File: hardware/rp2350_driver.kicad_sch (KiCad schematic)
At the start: 319 parts, among them J1 XT30, J10 Power Output, J11 CAN2 PLUG, J12 Conn_01x06, J2 XT30, J3 USB_C_Receptacle_USB2.0, J4 SM03B-SRSS-TB, J5 Estop Conn, J6 SM03B-SRSS-TB, J7 Conn_01x03, J8 Conn_01x03, J9 XT30, Q1 Q_PNP_BEC, Q2 Q_PNP_BEC, Q3 Q_PNP_BEC, Q4 Q_PNP_BEC, Q5 Q_NMOS_GDS, Q6 2N7002, SW1 Button, SW2 Button, U1 EG3113, U10 INA240A1D, U101 FUSB302BMPX, U11 USBLC6-2P6, U12 EG3113, U13 TS5A3159DCK, U14 TS5A3159DCK, U15 TS5A3159DCK, U16 CA-IS3052CG, U17 TS5A3159DCK, U18 SIT3088ETK, U19 SIT3088ETK, U20 SIT3088ETK, U21 SIT3088ETK, U22 TS5A3159DCK, U23 TS5A3159DCK, U24 TS5A3159DCK, U25 TS5A3159DCK, U26 TS5A3159DCK, U27 TS5A3159DCK, U28 XL7005A, U29 LM74700, U3 W25Q16JV, U30 TS5A3159DCK, U31 TS5A3159DCK, U32 TS5A3159DCK, U33 TS5A3159DCK, U4 SPX3819M5-L-3-3, U5 INA240A1D, U6 EG3113, U7 EG3113, U8 RP2350_80QFN, U9 INA240A1D, Y1 ABM8-272-T3

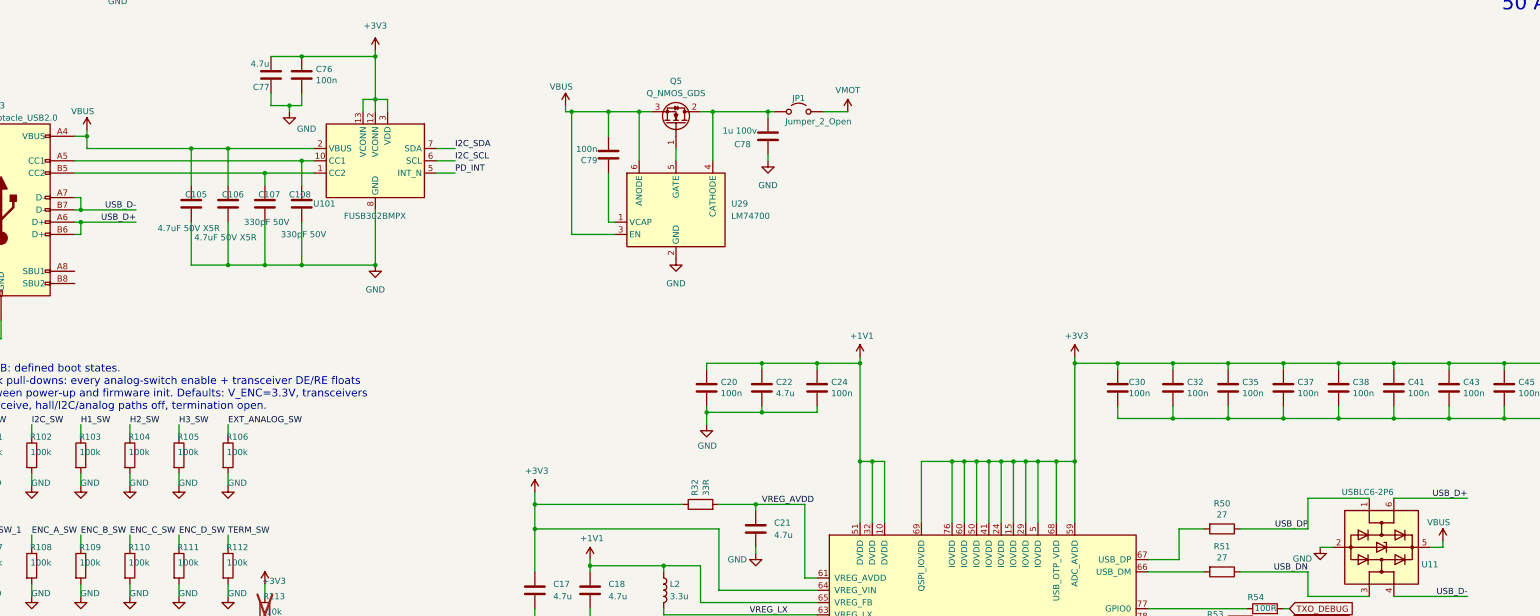
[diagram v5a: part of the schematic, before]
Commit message: rev-B schematic: LTC4359 USB power path (F-27) + U11/VBUS clamp fix (F-39)
First hardware change of the new rev. Both findings were rescoped to
rev-B on 2026-08-10 because the board's declared 5 A USB-PD capability
makes them shipping blockers, not respin nice-to-haves.

F-27 - the 65 V LM74700 was the weakest silicon on a 60 V bus, and at
5 A its companion FET was also a thermal fault:

  U29  LM74700 (SOT-23-6, 65 V abs max)  -> LTC4359CMS8 (MSOP-8, 4-80 V
       operating, 100 V abs-max pins, C688235)
  Q5   TMG08N10SI (SOT-89, 100 mohm, 2.5 W at 5 A)
       -> E100N4P0HL1 (PDFN5x6, 100 V, 4 mohm, 83 A, C29781176) ~0.1 W
  C79  removed - it was the LM74700 charge-pump cap; the LTC4359's pump
       is internal and the part needs no external cap here

Wired per the LTC4359 datasheet ideal-diode application: IN, SOURCE and
SHDN all at the input supply (SHDN tied to IN because shutdown is
unused, and the pin is rated to 100 V), GATE to the FET gate, OUT to
the drain, VSS to GND. FET orientation is unchanged - source to VBUS,
drain to the JP1/VMOT node - so the body diode still blocks backfeed.
Q5 moves to Device:Q_NMOS_SGD on parts:PowerPAK_SO-8_123, the same
symbol/footprint pair the bridge FETs use; the datasheet confirms
pins 1-3 = S, 4 = G, 5-8 = D, which is exactly that footprint's pad
numbering.

F-39 - U11 (USBLC6-2P6) referenced its data clamps to VBUS, a 5.5 V
abs-max pin sitting on a rail PD takes to 20 V:

  U11 pin 5 VBUS -> +3V3 (data lines clamp at ~4 V, correct for USB 2.0
      signalling, and the rail is always up when USB is active)
  D31 new SMAJ24A on VBUS at J3 (400 W, 24 V standoff, SMA, C148222),
      cathode to VBUS, anode to GND

Verified with kicad-cli: the net-level diff against the shipped rev-B
schematic contains these changes and nothing else, and ERC holds at the
baseline 278 violations (all pre-existing library-link noise).

Co-Authored-By: Claude Fable 5 <noreply@anthropic.com>
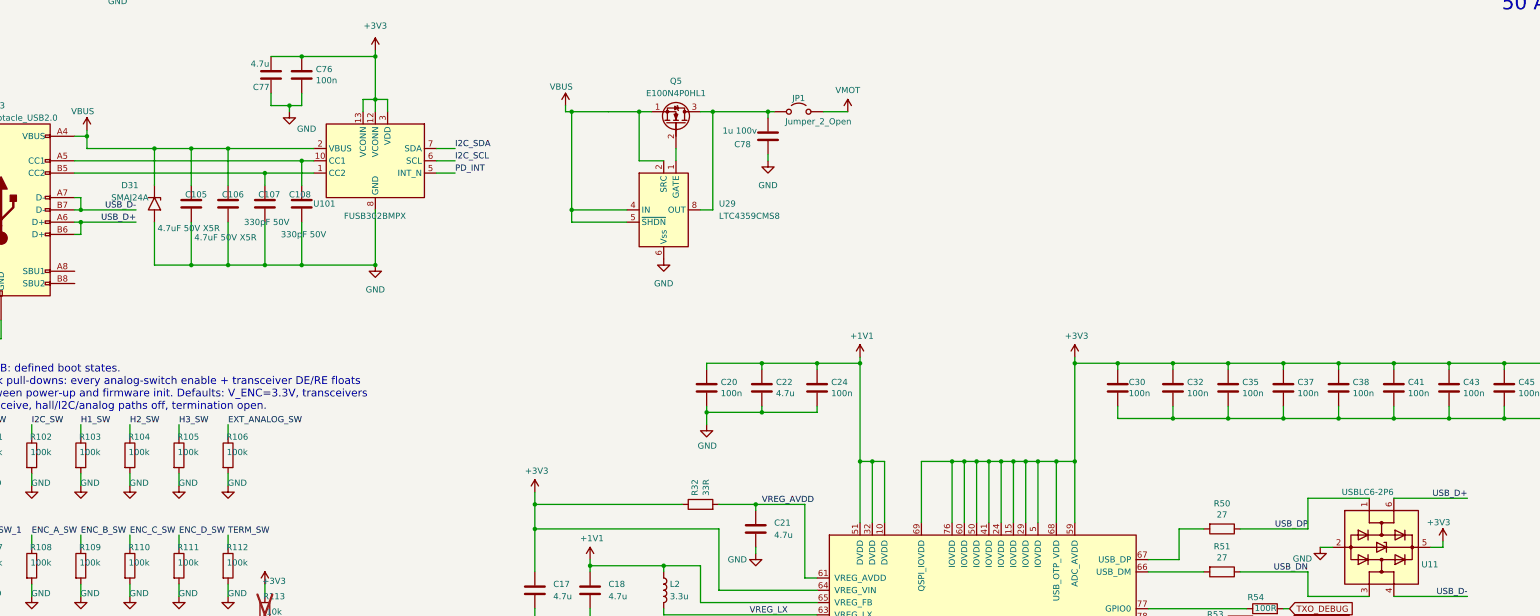
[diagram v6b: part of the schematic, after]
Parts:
- removed C79: 100n, Capacitor_SMD:C_0402_1005Metric, symbol Device:C
- added D31: SMAJ24A, Diode_SMD:D_SMA, symbol Diode:SMAJ24A
- Q5: value Q_NMOS_GDS -> E100N4P0HL1; footprint Package_TO_SOT_SMD:SOT-89-3 -> parts:PowerPAK_SO-8_123; symbol Transistor_FET:Q_NMOS_GDS -> Device:Q_NMOS_SGD; LCSC C7422896 -> C29781176
- U29: value LM74700 -> LTC4359CMS8; footprint Package_TO_SOT_SMD:SOT-23-6 -> Package_SO:MSOP-8_3x3mm_P0.65mm; symbol Power_Management:LM74700 -> Power_Management:LTC4359-MS8; LCSC C2941042 -> C688235
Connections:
- net +3V3: now also U11.5 (VBUS)
- net GND: now also U29.6 (Vss), D31.2 (A2); no longer U29.2 (GND)
- net VBUS: now also Q5.1 (S), U29.2 (SRC), U29.4 (IN), U29.5 (~{SHDN}), D31.1 (A1); no longer Q5.3 (S), U11.5 (VBUS), U29.3 (EN), U29.6 (ANODE)
- net at C78.2, JP1.1 (A): now also Q5.3 (D), U29.8 (OUT); no longer Q5.2 (D), U29.4 (CATHODE)
- net at U29.1 (GATE): now also Q5.2 (G)
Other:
- moved on the sheet: U29

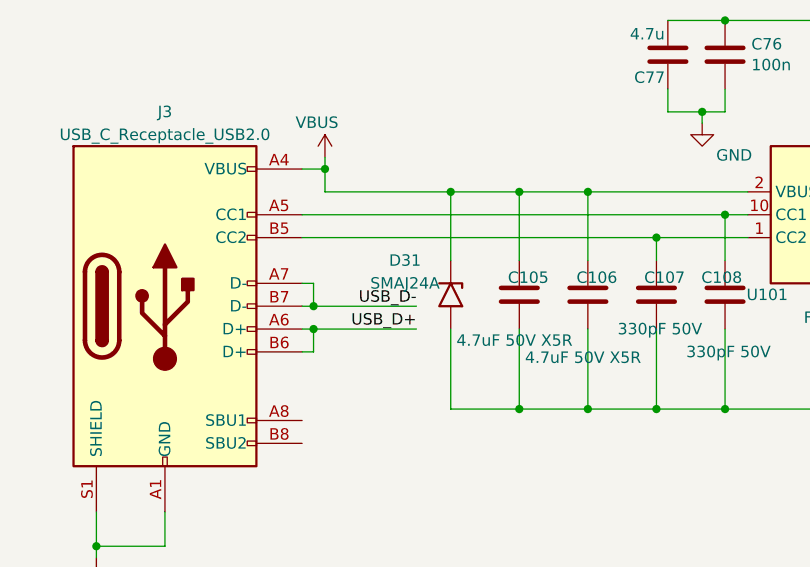
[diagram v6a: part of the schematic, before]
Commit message: rev-B PCB: sync F-27/F-39 to the schematic + placement (routing still due)
The schematic side of F-27/F-39 landed in 7058e41 with the PCB deliberately
left alone, on the read that both new footprints collided with five real
neighbours each and needed a placement session. That read was wrong: it counted
courtyards on the OPPOSITE copper side. U29 and Q5 are B.Cu parts, and most of
what looked like a collision (C45, C21, C24, R32, L2, C18, C17, C30, R50, R51)
is on F.Cu, where a courtyard cannot clash. Same-side, the job is small.

kicad-cli has no "update PCB from schematic" and pcbnew's SWIG bindings expose
no BOARD_NETLIST_UPDATER, so the sync is explicit, in tools/revb/:

  check_sync.py  exports the schematic netlist and diffs components, footprint
                 assignments and per-pad nets against the board. It classifies
                 the shipped board's pre-existing noise (27 footprints with no
                 library nickname, stale symbol-name values, unconnected-pad
                 naming, board-only thermal pads) instead of drowning in it.
                 This is the acceptance test, and it now says IN SYNC.
  scan_place.py  pose search. Drops the real footprint on the board at every
                 0.25 mm / 90 deg pose and asks KiCad for courtyards and pad
                 geometry. Hard constraints (same-side courtyard of a real
                 part, any other-net pad, board edge) must be zero; other-net
                 track segments crossed are the cost, since each is copper
                 someone must route again.
  sync_pcb.py    applies the delta, then verifies and refills before writing.

Placement chosen:

  U29  LTC4359 MSOP-8 at (167.745, 95.825) rot 0 - 1.00 mm east of the old
       SOT-23-6 centroid, rotated to horizontal into the space C79 vacated.
       Zero courtyard conflicts, zero test-point moves, zero extra copper.
  Q5   PowerPAK SO-8 at (170.400, 103.325) rot 180 - source east toward J3,
       drain west toward JP1, 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
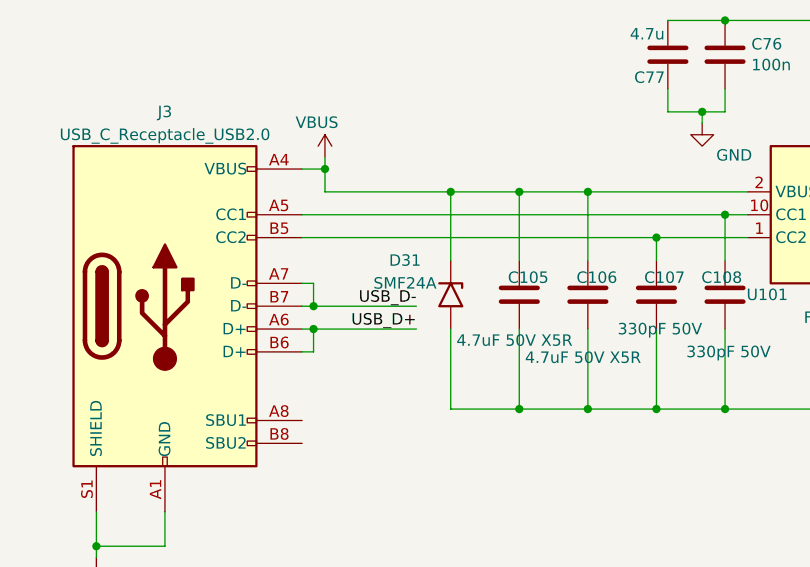
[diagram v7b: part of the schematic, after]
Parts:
- D31: value SMAJ24A -> SMF24A; footprint Diode_SMD:D_SMA -> Diode_SMD:D_SOD-123F; LCSC C148222 -> C169430
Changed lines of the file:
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@@
 			)
 		)
-		(property "Value" "SMAJ24A"
+		(property "Value" "SMF24A"
 			(at 93.98 104.14 90)
 			(effects
@@
 			)
 		)
-		(property "Footprint" "Diode_SMD:D_SMA"
+		(property "Footprint" "Diode_SMD:D_SOD-123F"
 			(at 99.06 105.41 90)
 			(effects
@@
 			)
 		)
-		(property "Datasheet" "https://www.littelfuse.com/media?resourcetype=datasheets&itemid=75e32973-b177-4ee3-a0ff-cedaf1abdb93&filename=smaj-datasheet"
+		(property "Datasheet" "https://www.littelfuse.com/assetdocs/tvs-diodes-smf-datasheet?assetguid=7eb8a5b6-bdd0-4561-8f19-0c3cc6f9b2af"
 			(at 99.06 105.41 0)
 			(effects
@@
 			)
 		)
-		(property "Description" "400W unidirectional TVS, 24 V standoff, SMA (DO-214AC) - VBUS surge clamp at J3"
+		(property "Description" "200W unidirectional TVS, 24 V standoff, SOD-123FL - VBUS surge clamp at J3"
 			(at 99.06 105.41 0)
 			(effects
@@
 			)
 		)
-		(property "LCSC" "C148222"
+		(property "LCSC" "C169430"
 			(at 99.06 105.41 0)
 			(effects

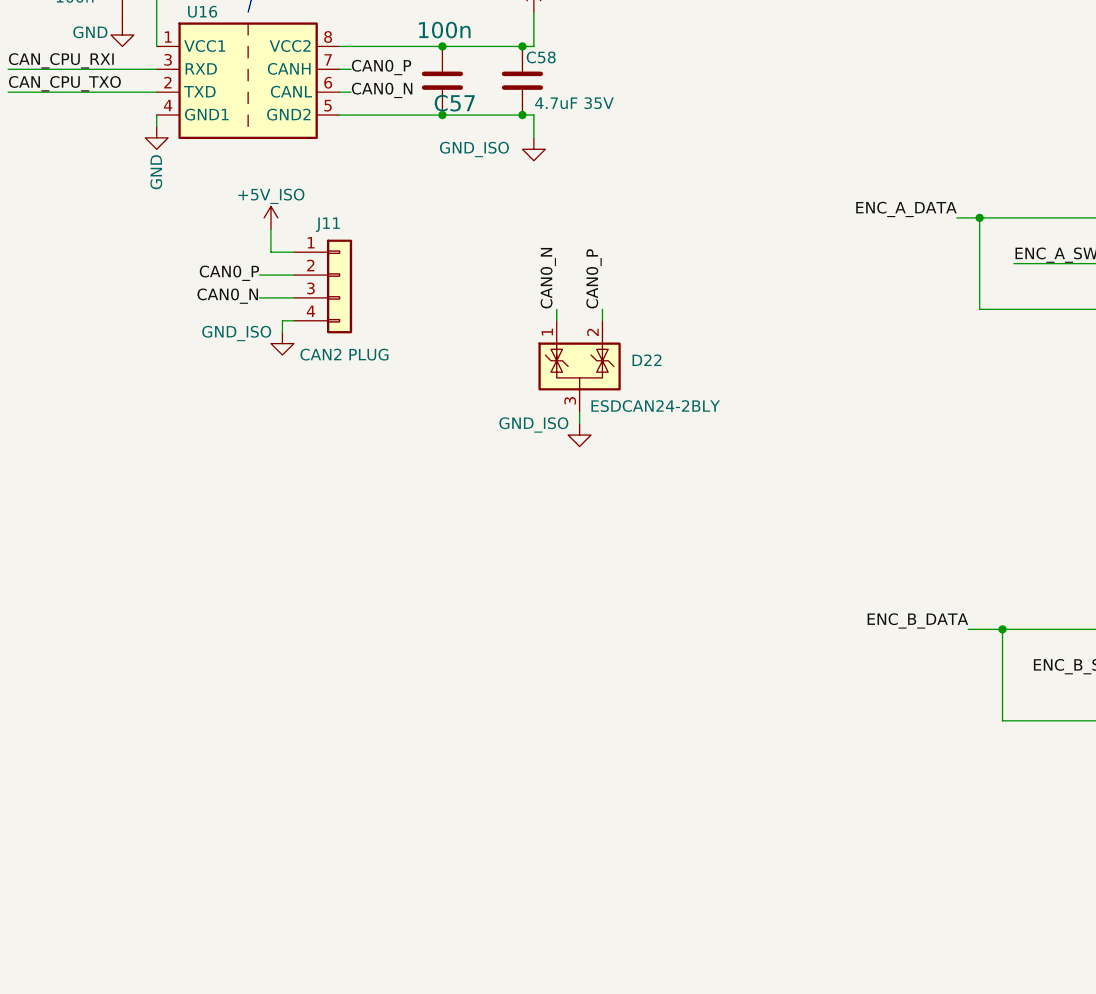
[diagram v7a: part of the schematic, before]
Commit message: rev-B: module-stretch verdict (F-44), rev-B parts re-placed + F-19 landed, Q6 SOT-23 (F-45), corner routed 238->54 airwires
Module stretch (review/modules.html, hardware/tools/modules/): the board carved
into 14 parent modules / 47 rigid leaves + 16 pinned interfaces; exact-polygon
slack probe, sequential-LP stretch, connectivity-owned copper warp, kicad DRC
referee. Verdict F-44: no module-level slack -- the DRC-neutral stretch is 5
loose parts (applied, signature-identical DRC); every dense-module move sheds
DRC violations through rule-pitch seam copper.

Placement: pose scanner on real KiCad geometry re-placed the 17 provisional
rev-B parts (U30-U33, C110-C113, R97-R100, R101/103/104/105/108), landed the
F-19 CAN parts (R114/JP2 by J11, C115 on the front between J11/J6, R115), and
swapped Q6 to the schematic's SOT-23 (F-45; check_sync known-exceptions now
empty). Corner cleanup removed the stray copper under the relaxed parts.

Routing: Freerouting with all copper locked hangs on this board; in-house
grid router (router.py) + GND plane stitching closed 197 of 251 connections.
Board: DRC 167 -> 4 (four cosmetic mask bridges), airwires 238 -> 54,
check_sync IN SYNC. F-25 stays open: the 54 left are named placement fixes.

Also lands the earlier uncommitted rev-B work on this branch: F-19 schematic
(add_f19_can_termination.py), F-43 0603->0402 shrink (shrink_0402.py), and
the F-19/F-42/F-43 register rows.

Co-Authored-By: Claude Fable 5 <noreply@anthropic.com>
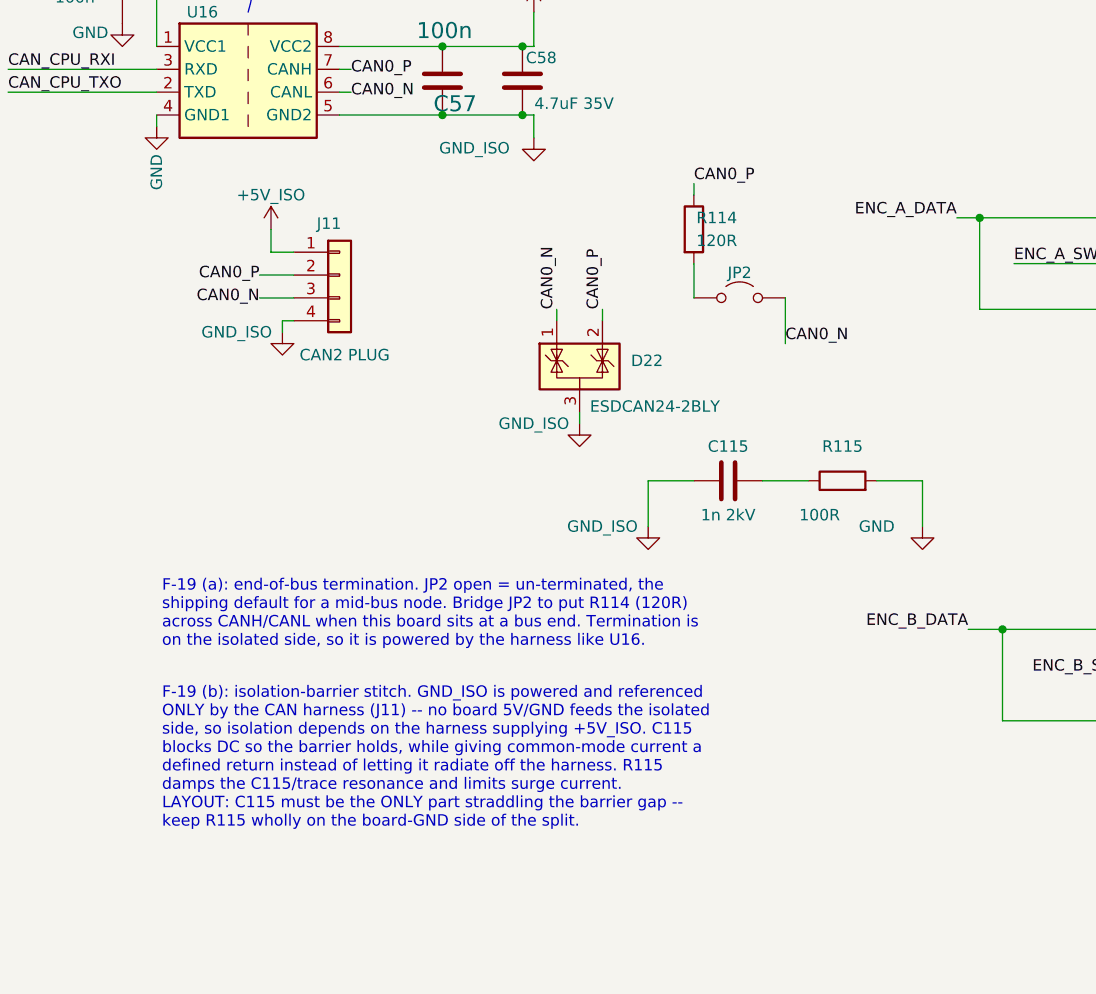
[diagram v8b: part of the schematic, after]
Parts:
- added C115: 1n 2kV, Capacitor_SMD:C_1206_3216Metric, symbol Device:C
- added JP2: Jumper_2_Open, Jumper:SolderJumper-2_P1.3mm_Open_RoundedPad1.0x1.5mm, symbol Jumper:Jumper_2_Open
- added R114: 120R, Resistor_SMD:R_0603_1608Metric, symbol Device:R
- added R115: 100R, Resistor_SMD:R_0603_1608Metric, symbol Device:R
- C16, C19, C29, C40: footprint Capacitor_SMD:C_0603_1608Metric -> Capacitor_SMD:C_0402_1005Metric
- R1, R2, R21, R22, R35, R36, R49, R53, R54, R65, R66: footprint Resistor_SMD:R_0603_1608Metric -> Resistor_SMD:R_0402_1005Metric
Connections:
- net CAN0_N: now also JP2.2 (B)
- net CAN0_P: now also R114.1
- net GND: now also R115.2
- net GND_ISO: now also C115.1
- new net: C115.2, R115.1
- new net: JP2.1 (A), R114.2
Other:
- note added: "F-19 (a): end-of-bus termination. JP2 open = un-terminated, the shipping default for a mid-bus node. Bridge JP2 to put R114 (120R) across CANH/CANL when this board sits at a bus end. Termination is on the isolated side, so it is powered by the harness like U16."
- note added: "F-19 (b): isolation-barrier stitch. GND_ISO is powered and referenced ONLY by the CAN harness (J11) -- no board 5V/GND feeds the isolated side, so isolation depends on the harness supplying +5V_ISO. C115 blocks DC so the barrier holds, while giving common-mode current a defined return instead of letting it radiate off the harness. R115 damps the C115/trace resonance and limits surge current. LAYO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"
